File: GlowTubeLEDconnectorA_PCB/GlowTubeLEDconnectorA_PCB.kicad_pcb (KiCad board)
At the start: 2 copper layers, 39.4 x 39.4 mm, 4 parts

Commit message: updated pcb design
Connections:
- LED1 pad 1: +5V -> GND
- LED1 pad 3: GND -> +5V
- LED3 pad 1: +5V -> GND
- LED3 pad 3: GND -> +5V
- LED4 pad 1: +5V -> GND
- LED4 pad 3: GND -> +5V
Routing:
- net +5V: track 69.7 -> 42.9 mm
- net LED1 DATA OUT: track 36.7 -> 33.1 mm
- net GND: track 60.2 -> 59.2 mm, vias 2 -> 0
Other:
- outline, holes or cut-outs redrawn

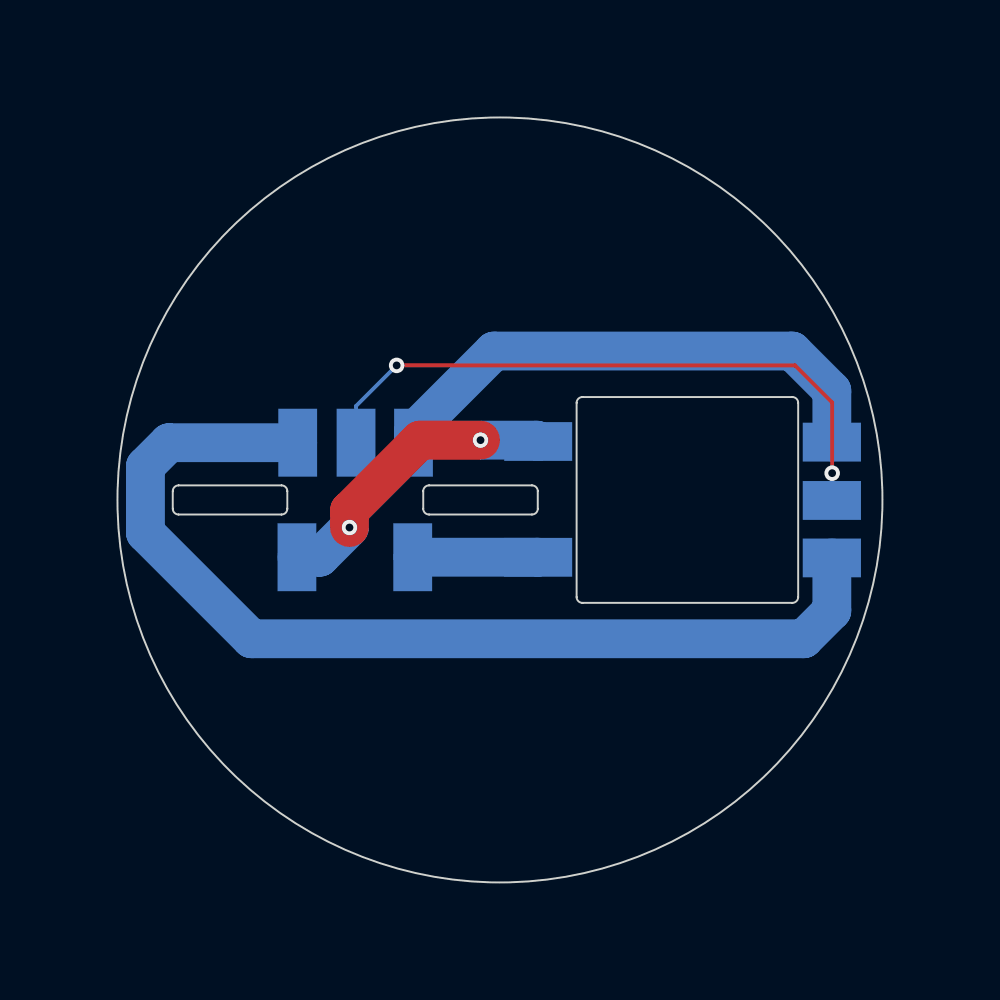
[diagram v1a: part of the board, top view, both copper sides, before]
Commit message: redesigned GlowTube PCBs
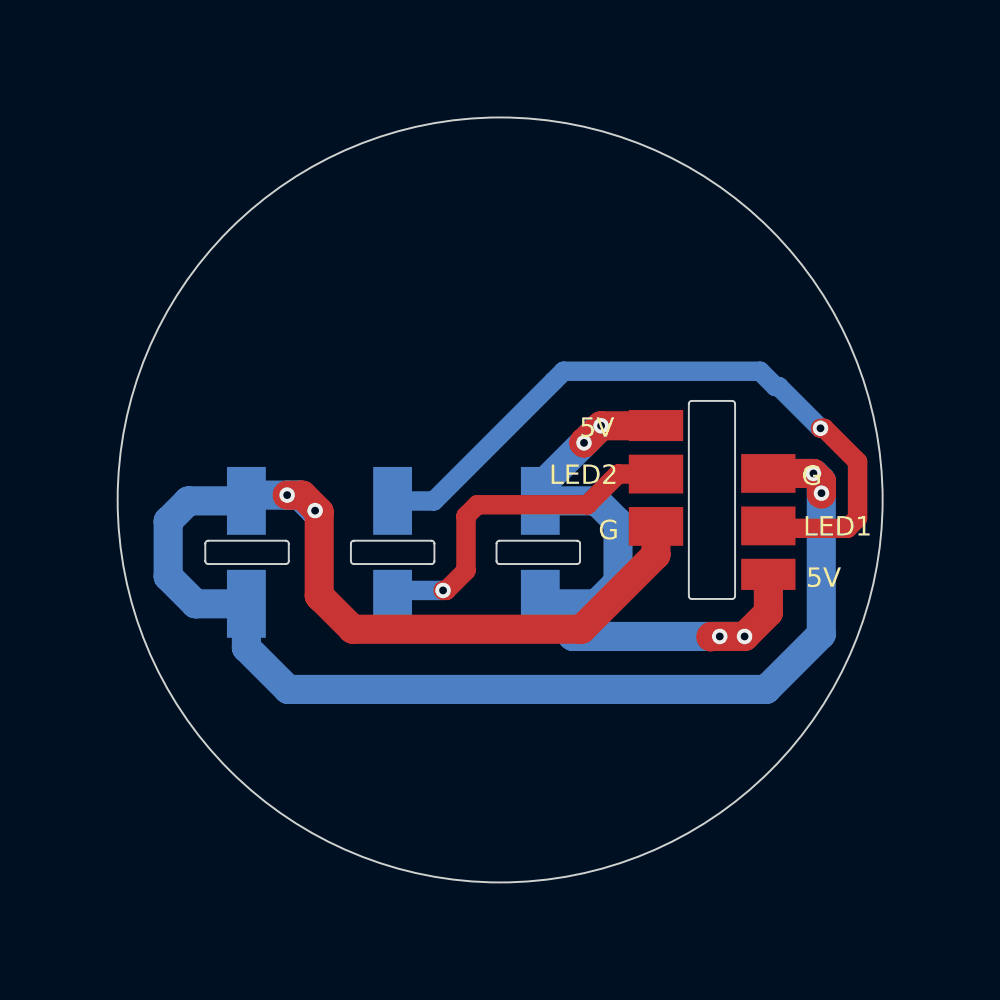
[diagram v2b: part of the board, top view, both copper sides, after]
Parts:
- removed LED1, LED2, LED3, LED4: LED_strip_contact_pads, Connector:LED strip connector pad
- added OSHW logo: OSHW-Logo2_7.3x6mm_SilkScreen, Symbol:OSHW-Logo2_7.3x6mm_SilkScreen, B.Cu at (112.3, 82.9)
- added P1: Solder_Pad, footprint:Solder pad, B.Cu at (105.0, 69.7)
- added P2: Solder_Pad, footprint:Solder pad, B.Cu at (97.4, 69.7)
- added P3: Solder_Pad, footprint:Solder pad, B.Cu at (89.9, 75.0)
- added P4: Solder_Pad, footprint:Solder pad, B.Cu at (105.0, 75.0)
- added P5: Solder_Pad, footprint:Solder pad, B.Cu at (97.4, 75.0)
- added P6: Solder_Pad, footprint:Solder pad, B.Cu at (89.9, 69.7)
- added U1: Contact pads, myparts:LED strip connector 4pad small, F.Cu at (116.8, 69.7)
- added U2: Contact pads, myparts:LED strip connector 4pad small, F.Cu at (111.0, 69.7)
- added designedby: LOGO, LOGO, B.Cu at (98.9, 83.3)
- added qrcode: LOGO, LOGO, B.Cu at (94.0, 60.8)
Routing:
- net GND: track 59.2 -> 89.4 mm, vias 0 -> 4
- net LED2 DATA OUT: track 0.00 -> 18.0 mm, vias 0 -> 1
- net +5V: track 42.9 -> 38.1 mm, vias 2 -> 4
- net LED1 DATA OUT: track 33.1 -> 36.4 mm, vias 2 -> 1
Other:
- outline, holes or cut-outs redrawn
- board text added: "5V"
- board text added: "Connector A PCB v1.0 beta 2"
- board text added: "G"
- board text added: "GND"
- board text added: "GlowTube"
- board text added: "LED1"
- board text added: "LED2"
- board text added: "PCB files: https://bit.ly/3LUCy3a"

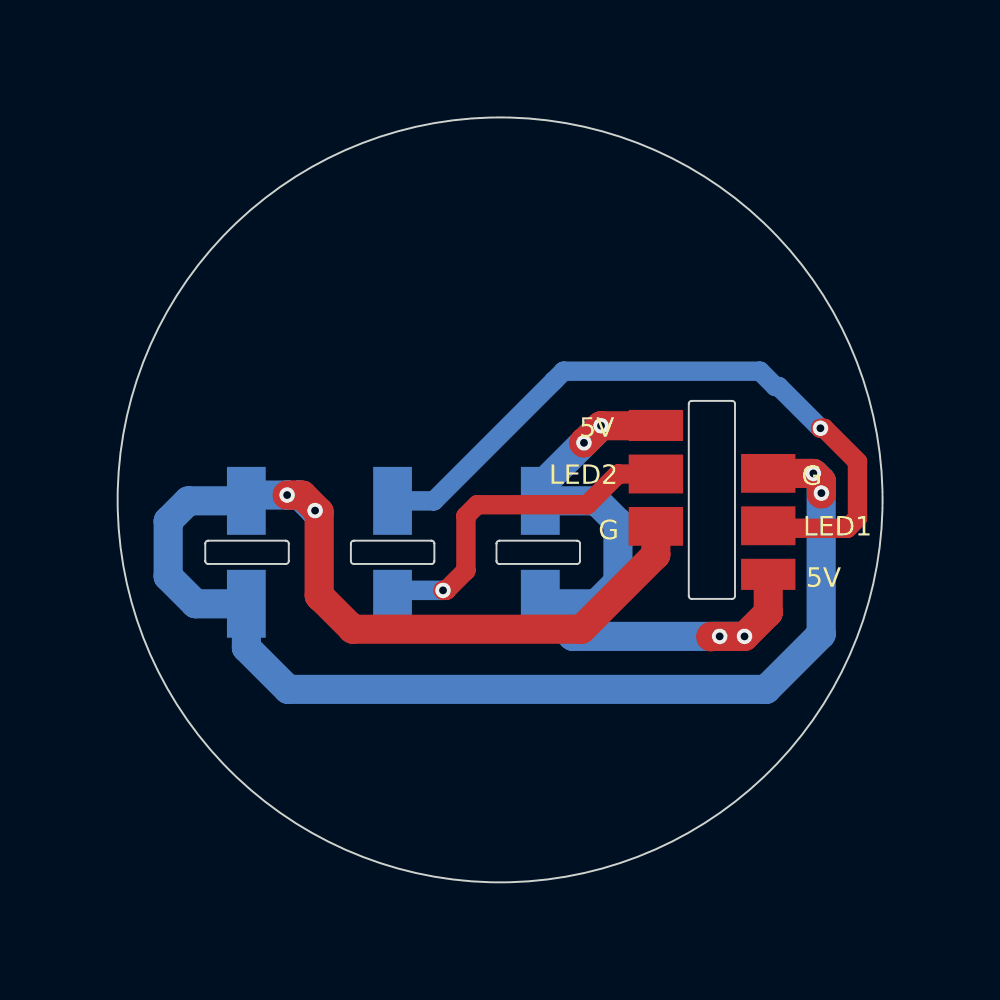
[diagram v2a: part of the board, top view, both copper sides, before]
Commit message: updated PCB designs to release candidate 1
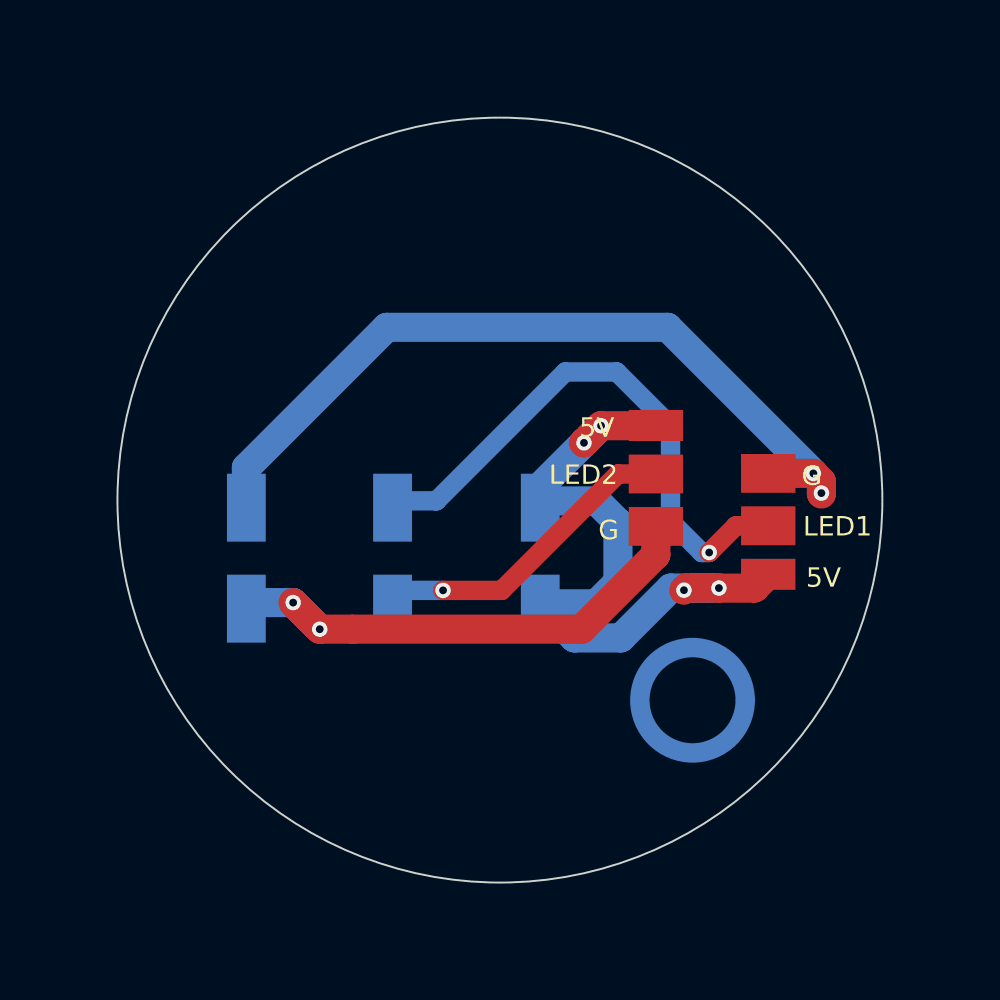
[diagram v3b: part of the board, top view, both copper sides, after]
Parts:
- removed OSHW logo: OSHW-Logo2_7.3x6mm_SilkScreen, Symbol:OSHW-Logo2_7.3x6mm_SilkScreen
- added U3: SMTSO3015CTJ, footprint:SMTSO3030CTJ, B.Cu at (112.9, 80.0)
- moved qrcode 15.7 mm to (109.7, 59.7)
- moved P1 0.35 mm to (105.0, 70.0)
- moved P2 0.35 mm to (97.4, 70.0)
- moved P6 0.35 mm to (89.9, 70.0)
- moved P3 0.25 mm to (89.9, 75.2)
- moved P4 0.25 mm to (105.0, 75.2)
- moved P5 0.25 mm to (97.4, 75.2)
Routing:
- net GND: track 89.4 -> 67.3 mm
- net LED1 DATA OUT: track 36.4 -> 29.6 mm
- net LED2 DATA OUT: track 18.0 -> 16.3 mm
- net +5V: track 38.1 -> 37.1 mm
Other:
- outline, holes or cut-outs redrawn
- board text added: "Connector A PCB v1.0 RC1"
- board text removed: "Connector A PCB v1.0 beta 2"

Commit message: updated pcbs
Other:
- board text added: "Connector A PCB v1.0"
- board text removed: "Connector A PCB v1.0 RC1"
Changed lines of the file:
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@@
       (effects (font (size 1 1) (thickness 0.15)) (justify mirror))
     )
+    (pad "" np_thru_hole circle (at 0.00997 -0.00254 180) (size 4.3 4.3) (drill 4.3) (layers F&B.Cu *.Mask))
     (pad "1" smd custom (at -2.7178 0 180) (size 1 1) (layers "B.Cu" "B.Paste" "B.Mask")
       (net 5 "unconnected-(U3-Pad1)") (pinfunction "1") (pintype "unspecified")
@@
       ))
     (model "${GLOWINGKITTYPARTS}/footprint/packages3d/SMTSO3030CTJ.step"
-      (offset (xyz 0 0 0))
+      (offset (xyz 0 0 3))
       (scale (xyz 1 1 1))
-      (rotate (xyz 0 0 0))
+      (rotate (xyz 0 180 0))
     )
   )
@@
       (effects (font (size 1 1) (thickness 0.15)) (justify mirror))
     )
-    (pad "1" smd rect locked (at -0.0762 -0.0508 180) (size 2 3.5) (layers "B.Cu" "B.Mask")
+    (pad "1" smd rect (at -0.0762 -0.0508 180) (size 2 3.5) (layers "B.Cu" "B.Mask")
       (net 3 "GND") (pintype "bidirectional"))
   )
@@
       (effects (font (size 1 1) (thickness 0.15)) (justify mirror))
     )
-    (pad "1" smd rect locked (at -0.0762 -0.0508 180) (size 2 3.5) (layers "B.Cu" "B.Mask")
+    (pad "1" smd rect (at -0.0762 -0.0508 180) (size 2 3.5) (layers "B.Cu" "B.Mask")
       (net 1 "+5V") (pintype "bidirectional"))
   )
@@
       (effects (font (size 1 1) (thickness 0.15)) (justify mirror))
     )
-    (pad "1" smd rect locked (at -0.0762 -0.0508 180) (size 2 3.5) (layers "B.Cu" "B.Mask")
+    (pad "1" smd rect (at -0.0762 -0.0508 180) (size 2 3.5) (layers "B.Cu" "B.Mask")
       (net 3 "GND") (pintype "bidirectional"))
   )
@@
       (effects (font (size 1 1) (thickness 0.15)) (justify mirror))
     )
-    (pad "1" smd rect locked (at -0.0762 -0.0508 180) (size 2 3.5) (layers "B.Cu" "B.Mask")
+    (pad "1" smd rect (at -0.0762 -0.0508 180) (size 2 3.5) (layers "B.Cu" "B.Mask")
       (net 2 "LED1 DATA OUT") (pintype "bidirectional"))
   )
@@
       (effects (font (size 1 1) (thickness 0.15)) (justify mirror))
     )
-    (pad "1" smd rect locked (at -0.0762 -0.0508 180) (size 2 3.5) (layers "B.Cu" "B.Mask")
+    (pad "1" smd rect (at -0.0762 -0.0508 180) (size 2 3.5) (layers "B.Cu" "B.Mask")
       (net 4 "LED2 DATA OUT") (pintype "bidirectional"))
   )
@@
       (effects (font (size 1 1) (thickness 0.15)) (justify mirror))
     )
-    (pad "1" smd rect locked (at -0.0762 -0.0508 180) (size 2 3.5) (layers "B.Cu" "B.Mask")
+    (pad "1" smd rect (at -0.0762 -0.0508 180) (size 2 3.5) (layers "B.Cu" "B.Mask")
       (net 1 "+5V") (pintype "bidirectional"))
   )
@@
   (gr_rect (start 112.25 64.65) (end 115.63 74.65) (layer "User.3") (width 0.1) (fill none))
   (gr_rect (start 84.13 71.81) (end 121 73.51) (layer "User.3") (width 0.1) (fill none))
-  (gr_text "Connector A PCB \nv1.0 RC1" (at 104.26 62.75) (layer "B.SilkS")
+  (gr_text "Connector A PCB \nv1.0" (at 104.26 62.75) (layer "B.SilkS")
     (effects (font (size 1 1) (thickness 0.15)) (justify left mirror))
   )
